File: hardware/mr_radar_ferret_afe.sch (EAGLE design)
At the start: 66 parts, among them U1 GALI-55+, U10 MAX2750, U11 GALI-55+, U12 AD5621, U13 REF2930, U3 GALI-55+, U4 GALI-55+, U7 DC25-73, U8 HMC213

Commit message: split adc front-end to another board, changed microstrip for 1.6mm thick board
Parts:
- removed C1, C9: DNP, pel_dipol_comp:CAPACITOR-0603
- removed C11, C12: 220pF, pel_dipol_comp:CAPACITOR-0603
- removed C13, C14, C20, C32, C35, C38, C41: 100nF, pel_dipol_comp:CAPACITOR-0603
- removed C15, C31, C34, C37, C40: 10nF, pel_dipol_comp:CAPACITOR-0603
- removed C16, C17, C2, C3, C43, C5, C6, C7, C8: 39pF, pel_dipol_comp:CAPACITOR-0603
- removed C26, C27: .1uF, pel_dipol_comp:CAPACITOR-0603
- removed C30, C4, C44: 10uF, pel_dipol_comp:CAPACITOR-POLA
- removed C33, C36, C39, C42: 100pF, pel_dipol_comp:CAPACITOR-0603
- removed J$1, J$2, J$4, J$5: SMA_EDGE, SparkFun-Connectors:SMA_EDGE
- removed JP1: (no value), SparkFun-Connectors:M05PTH
- removed JP3: (no value), SparkFun-Connectors:M03SCREW
- removed L1, L2, L3, L4: 10nH, pel_dipol_comp:INDUCTOR-0603
- removed R1, R2, R22, R23, R3, R4: 110, pel_dipol_comp:RESISTOR-0603
- removed R10, R11, R12, R5: JMP, pel_dipol_comp:RESISTOR-0603
- removed TP3: TPTP14SQ, testpad:TPTP14SQ
- removed U$14, U$2: 2450BP39C100CE, retro:2450BP39C100CE
- removed U1, U11, U3, U4: GALI-55+, retro:GALI-55+
- removed U10: MAX2750, retro:MAX2750
- removed U12: AD5621, retro:AD5621
- removed U13: REF2930, retro:REF2930
- removed U7: DC25-73, retro:DC25-73
- removed U8: HMC213, retro:HMC213
- added C10, C45: 10uF, pel_dipol_comp:CAPACITOR-POLA
- added C18, C19, C24: 100nF, pel_dipol_comp:CAPACITOR-0603
- added C21: 1uF, pel_dipol_comp:CAPACITOR-0603
- added C22: DNP, pel_dipol_comp:CAPACITOR-0603
- added C23: 2nH, pel_dipol_comp:CAPACITOR-0603
- added C25: 100nH, pel_dipol_comp:CAPACITOR-0603
- added C28, C29: .1uF, pel_dipol_comp:CAPACITOR-0603
- added J$3, J$6: SMA_EDGE, SparkFun-Connectors:SMA_EDGE
- added JP2: (no value), SparkFun-Connectors:M06SIP
- added JP4: (no value), SparkFun-Connectors:M03SCREW
- added R13, R14, R15, R16, R17, R18, R19, R20, R21, R9: JMP, pel_dipol_comp:RESISTOR-0603
- added R6, R8: 100, pel_dipol_comp:RESISTOR-0603
- added R7: 2k, pel_dipol_comp:RESISTOR-0603
- added TP1: TPTP14SQ, testpad:TPTP14SQ
- added U16: AD7276, retro:AD7276
- added U18: REF2930, retro:REF2930
- added U5, U6: MAX9812, retro:MAX9812
- added U9: MAX7410, retro:MAX7410
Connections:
- removed net +10V: C34.1, C35.1, C36.1, C37.1, C38.1, C39.1, C44.+, JP3.2, R22.2, R3.2, R4.2
- removed net N$10: C5.1, U7.CPL@3
- removed net N$11: C5.2, U3.RFIN
- removed net N$12: L2.1, R2.1
- removed net N$13: C6.1, L2.2, U3.RFOUT
- removed net N$14: C6.2, U8.LO@2
- removed net N$15: C17.1, U8.RF@7
- removed net N$16: L4.1, R4.1
- removed net N$17: L3.1, R3.1
- removed net N$18: C7.1, L3.2, U4.RFOUT
- removed net N$19: C7.2, U11.RFIN
- removed net N$2: L1.1, R1.1
- removed net N$20: C8.1, L4.2, U11.RFOUT
- removed net N$21: C8.2, U$2G$1.P$1
- removed net N$22: R5.2, U8.IF@5
- removed net N$24: C13.1, U10.BYP@1
- removed net N$26: C1.1, R12.2, U10.TUNE@2
- removed net N$27: C16.2, J$1.SIGNAL
- removed net N$28: C16.1, U$2G$1.P$2
- removed net N$29: C17.2, U4.RFIN
- removed net N$3: C2.1, L1.2, U1.RFOUT
- removed net N$30: C3.1, U$14G$1.P$2
- removed net N$39: C9.1, J$5.SIGNAL, R5.1
- removed net N$4: C2.2, U$14G$1.P$1
- removed net N$41: C26.1, U12.VDD@4, U13.VREF@2
- removed net N$45: JP1.1, U12.SDIN@3
- removed net N$46: JP1.2, U12.SCLK@2
- removed net N$47: JP1.3, U12.!SYNC@1
- removed net N$48: C31.1, C32.1, C33.1, C40.1, C41.1, C42.1, R1.2, R2.2, R22.1, R23.1
- removed net N$5: C43.2, U1.RFIN
- removed net N$50: C43.1, U10.OUT@7
- removed net N$54: JP1.5, R11.2, U12.VOUT@6
- removed net N$6: C3.2, U7.IN@4
- removed net N$7: J$2.SIGNAL, U7.OUT@6
- removed net N$8: R10.1, TP3.TP, U10.!SHDN@4
- removed net VTUNE: J$4.SIGNAL, R11.1, R12.1
- new net COM: C25.1, TP1.TP, U9.COM@1, U9.OS@6
- new net N$1: C10.-, R7.2, R8.1, U6.IN@6
- new net N$23: C10.+, J$6.SIGNAL, R6.1
- new net N$25: JP2.4, R16.2
- new net N$31: R9.1, U6.!SHDN@1
- new net N$32: R13.1, U5.!SHDN@1
- new net N$33: C21.1, U5.OUT@3
- new net N$34: C21.2, U9.IN@2
- new net N$35: C22.1, J$3.SIGNAL, R14.1, R17.2, R18.2
- new net N$36: R14.2, U9.OUT@5
- new net N$37: R15.2, R16.1, U9.CLK@8
- new net N$38: C23.1, R15.1
- new net N$40: R7.1, U6.BIAS@5
- new net N$42: JP2.3, U16.SCLK@4
- new net N$43: JP2.1, U16.!CS@6
- new net N$44: JP2.2, U16.SDATA@5
- new net N$49: C28.1, U16.VDD@1, U18.VREF@2
- new net N$51: JP2.6, R18.1
- new net N$52: R17.1, R19.2, R20.1
- new net N$53: R20.2, R21.1, U16.VIN@3
- new net N$9: U5.IN@6, U6.OUT@3
- net +5V: now also C18.1, C19.1, C24.1, C29.1, C45.+, JP4.2, R13.2, R9.2, U18.IN@1, U5.VCC@4, U6.VCC@4, U9.!SHDN@7, U9.VDD@4; no longer C11.1, C12.1, C14.1, C15.1, C20.1, C27.1, C30.+, C4.+, JP3.3, R10.2, R23.2, U10.VCC1@5, U10.VCC2@6, U13.IN@1
- net GND: now also C18.2, C19.2, C22.2, C23.2, C24.2, C25.2, C28.2, C29.2, C45.-, J$3.GND@0, J$3.GND@1, J$3.GND@2, J$3.GND@3, J$6.GND@0, J$6.GND@1, J$6.GND@2, J$6.GND@3, JP2.5, JP4.1, JP4.3, R19.1, R21.2, R6.2, R8.2, U16.GND@2, U18.GND@3, U5.GND@2, U6.GND@2, U9.GND@3; no longer C1.2, C11.2, C12.2, C13.2, C14.2, C15.2, C20.2, C26.2, C27.2, C30.-, C31.2, C32.2, C33.2, C34.2, C35.2, C36.2, C37.2, C38.2, C39.2, C4.-, C40.2, C41.2, C42.2, C44.-, C9.2, J$1.GND@0, J$1.GND@1, J$1.GND@2, J$1.GND@3, J$2.GND@0, J$2.GND@1, J$2.GND@2, J$2.GND@3, J$4.GND@0, J$4.GND@1, J$4.GND@2, J$4.GND@3, J$5.GND@0, J$5.GND@1, J$5.GND@2, J$5.GND@3, JP1.4, JP3.1, U1.GND@0, U1.GND@1, U10.GND@3, U10.GND@8, U11.GND@0, U11.GND@1, U12.GND@5, U13.GND@3, U3.GND@0, U3.GND@1, U4.GND@0, U4.GND@1, U7.GND@1, U7.GND@2, U7.GND@5, U8.GND@1, U8.GND@3, U8.GND@6, U8.GND@8, U8.NC@4

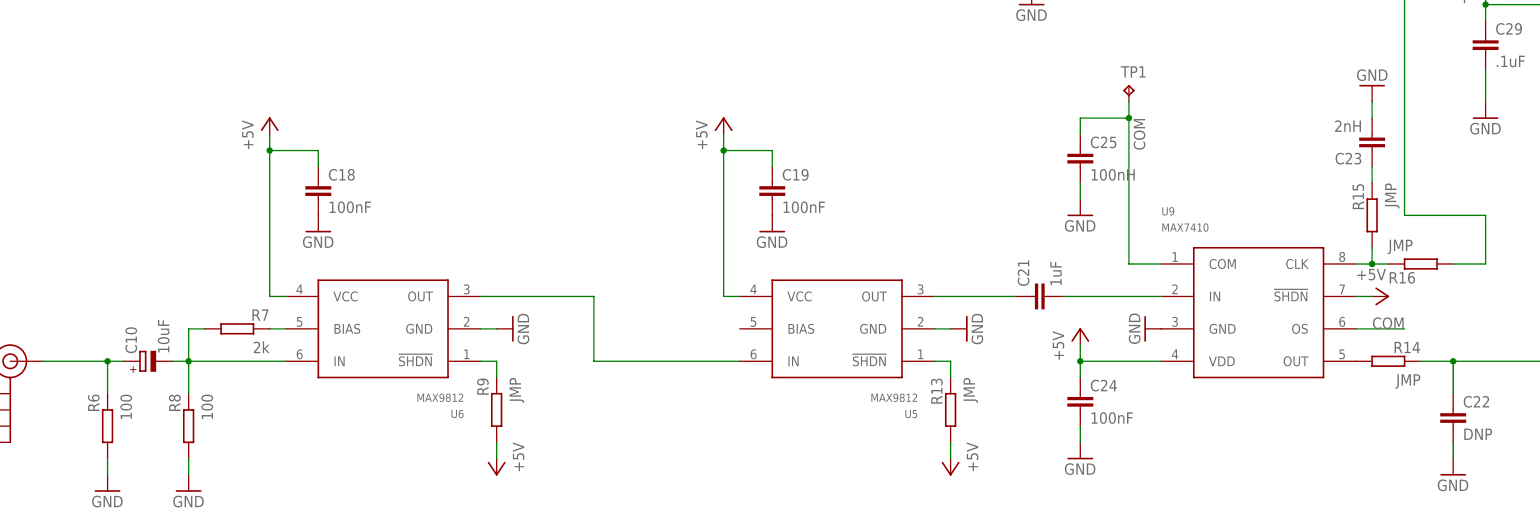
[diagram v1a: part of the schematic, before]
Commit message: currently tested ferret r0, fixing a few bugs for the next revision, board layout of ferret now incomplete. isolation is much better than in platypus, but it is still a problem
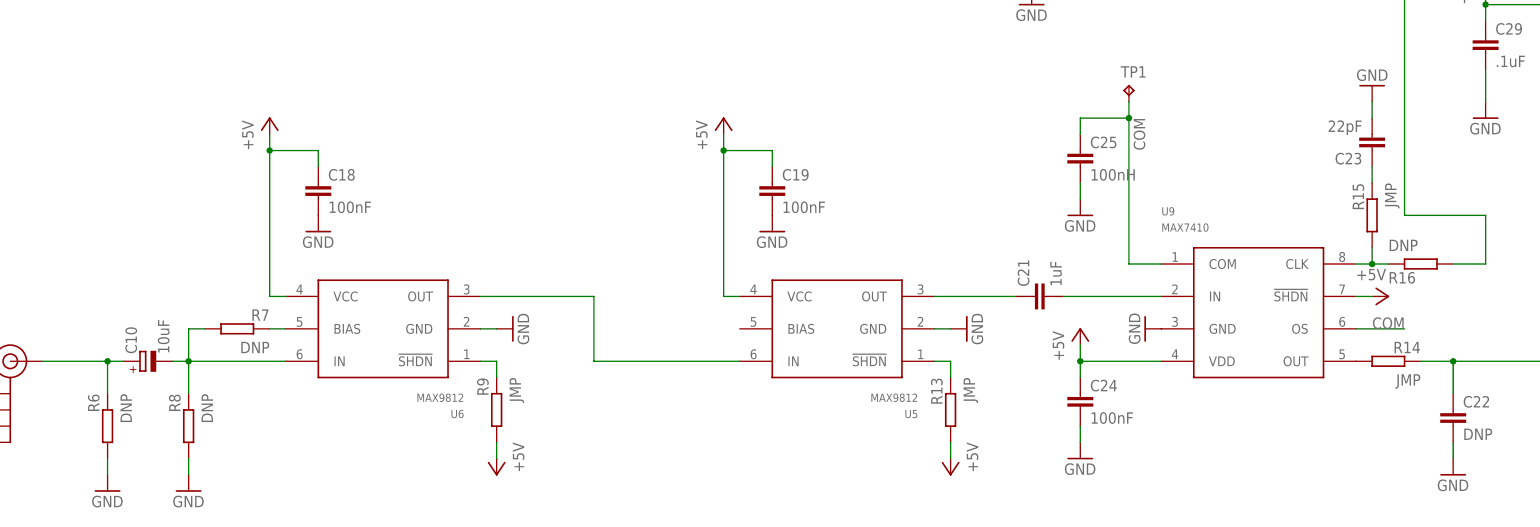
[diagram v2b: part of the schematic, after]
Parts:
- C23: value 2nH -> 22pF
- R16: value JMP -> DNP
- R6, R8: value 100 -> DNP
- R7: value 2k -> DNP
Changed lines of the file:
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@@
 <part name="U9" library="retro" deviceset="MAX7410" device=""/>
 <part name="J$3" library="SparkFun-Connectors" deviceset="SMA_EDGE" device=""/>
-<part name="R6" library="pel_dipol_comp" deviceset="RESISTOR" device="-0603" value="100"/>
+<part name="R6" library="pel_dipol_comp" deviceset="RESISTOR" device="-0603" value="DNP"/>
 <part name="GND14" library="supply1" deviceset="GND" device=""/>
 <part name="GND16" library="supply1" deviceset="GND" device=""/>
@@
 <part name="R14" library="pel_dipol_comp" deviceset="RESISTOR" device="-0603" value="JMP"/>
 <part name="GND24" library="supply1" deviceset="GND" device=""/>
-<part name="C23" library="pel_dipol_comp" deviceset="CAPACITOR" device="-0603" value="2nH"/>
+<part name="C23" library="pel_dipol_comp" deviceset="CAPACITOR" device="-0603" value="22pF"/>
 <part name="R15" library="pel_dipol_comp" deviceset="RESISTOR" device="-0603" value="JMP"/>
 <part name="GND32" library="supply1" deviceset="GND" device=""/>
-<part name="R16" library="pel_dipol_comp" deviceset="RESISTOR" device="-0603" value="JMP"/>
+<part name="R16" library="pel_dipol_comp" deviceset="RESISTOR" device="-0603" value="DNP"/>
 <part name="P+10" library="supply1" deviceset="+5V" device=""/>
 <part name="C24" library="pel_dipol_comp" deviceset="CAPACITOR" device="-0603" value="100nF"/>
 <part name="P+11" library="supply1" deviceset="+5V" device=""/>
 <part name="GND33" library="supply1" deviceset="GND" device=""/>
-<part name="R7" library="pel_dipol_comp" deviceset="RESISTOR" device="-0603" value="2k"/>
+<part name="R7" library="pel_dipol_comp" deviceset="RESISTOR" device="-0603" value="DNP"/>
 <part name="C25" library="pel_dipol_comp" deviceset="CAPACITOR" device="-0603" value="100nH"/>
 <part name="GND34" library="supply1" deviceset="GND" device=""/>
@@
 <part name="J$6" library="SparkFun-Connectors" deviceset="SMA_EDGE" device=""/>
 <part name="GND64" library="supply1" deviceset="GND" device=""/>
-<part name="R8" library="pel_dipol_comp" deviceset="RESISTOR" device="-0603" value="100"/>
+<part name="R8" library="pel_dipol_comp" deviceset="RESISTOR" device="-0603" value="DNP"/>
 <part name="GND66" library="supply1" deviceset="GND" device=""/>
 <part name="JP4" library="SparkFun-Connectors" deviceset="M03" device="SCREW"/>
